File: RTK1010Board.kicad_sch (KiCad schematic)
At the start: 71 parts, among them J1 SMA, J2 IPEX, J3 USB_OTG, J4 BNO055, U1 RTK-1010, U2 MCP1700-3002E_SOT23, U3 MCP1700-3002E_SOT23, U4 ESP32-S2-WROVER

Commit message: some optimiziations implemented
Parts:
- added C12: 10uF, Capacitor_Tantalum_SMD:CP_EIA-7132-20_AVX-U_Pad2.72x3.50mm_HandSolder, symbol Device:C_Polarized_Small
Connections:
- net 5V is gone; now on net U5: JP2.2 (B)
- net GND: now also C12.2
- net U5: now also C12.1
- no-connect marks 25 -> 35
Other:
- note added: "BNO055 IMU (Optional)"
- moved on the sheet: J4, R17, R18

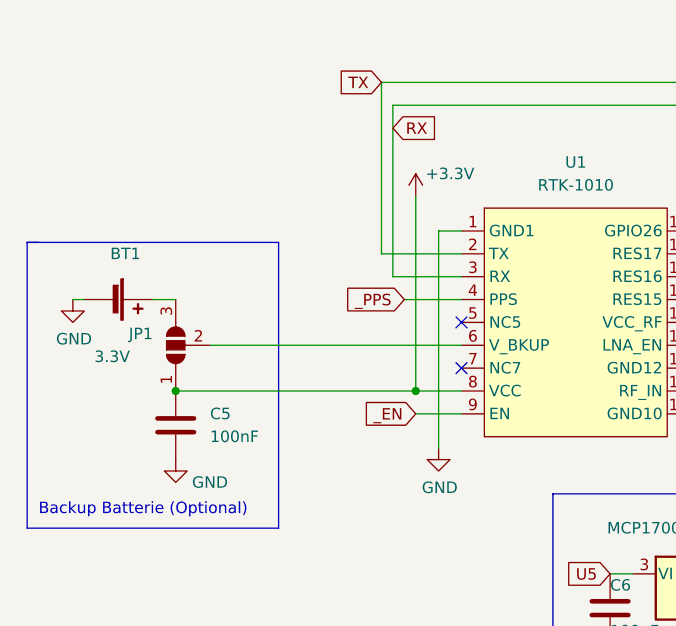
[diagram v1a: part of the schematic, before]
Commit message: RTK1010 VCC LP filter added
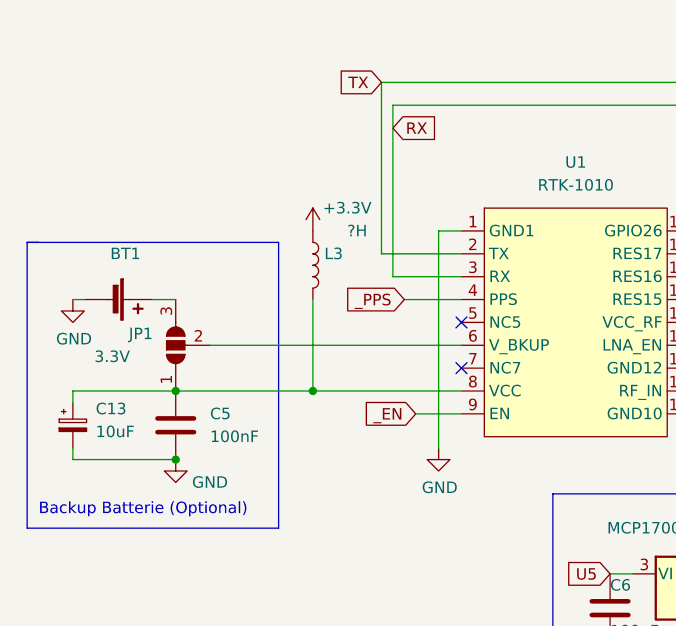
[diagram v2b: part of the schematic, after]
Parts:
- added C13: 10uF, Capacitor_Tantalum_SMD:CP_EIA-7132-20_AVX-U_Pad2.72x3.50mm_HandSolder, symbol Device:C_Polarized_Small
- added L3: ?H, Inductor_SMD:L_0805_2012Metric_Pad1.15x1.40mm_HandSolder, symbol Device:L
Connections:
- net +3V3: now also L3.1; no longer C5.1, JP1.1 (A), U1.8 (VCC)
- net GND: now also C13.2
- new net: C13.1, C5.1, JP1.1 (A), L3.2, U1.8 (VCC)
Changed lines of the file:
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@@
   (junction (at 88.9 85.09) (diameter 0) (color 0 0 0 0)
   )
-  (junction (at 57.15 57.15) (diameter 0) (color 0 0 0 0)
-  )
   (junction (at 275.59 157.48) (diameter 0) (color 0 0 0 0)
   )
@@
   (junction (at 60.96 189.23) (diameter 0) (color 0 0 0 0)
   )
+  (junction (at 45.72 57.15) (diameter 0) (color 0 0 0 0)
+  )
   (junction (at 251.46 157.48) (diameter 0) (color 0 0 0 0)
   )
@@
   (junction (at 177.8 66.04) (diameter 0) (color 0 0 0 0)
   )
+  (junction (at 30.48 64.77) (diameter 0) (color 0 0 0 0)
+  )
   (junction (at 280.67 157.48) (diameter 0) (color 0 0 0 0)
   )
@@
     (stroke (width 0) (type default) (color 0 0 0 0))
   )
-  (wire (pts (xy 57.15 57.15) (xy 62.23 57.15))
+  (wire (pts (xy 30.48 57.15) (xy 45.72 57.15))
     (stroke (width 0) (type default) (color 0 0 0 0))
   )
@@
     (stroke (width 0) (type default) (color 0 0 0 0))
   )
+  (wire (pts (xy 45.72 57.15) (xy 62.23 57.15))
+    (stroke (width 0) (type default) (color 0 0 0 0))
+  )
   (wire (pts (xy 201.93 121.92) (xy 208.28 121.92))
     (stroke (width 0) (type default) (color 0 0 0 0))
@@
     (stroke (width 0) (type default) (color 0 0 0 0))
   )
-  (wire (pts (xy 57.15 35.56) (xy 57.15 57.15))
-    (stroke (width 0) (type default) (color 0 0 0 0))
-  )
   (polyline (pts (xy 233.68 134.62) (xy 233.68 97.79))
     (stroke (width 0) (type default) (color 0 0 0 0))
@@
     (stroke (width 0) (type default) (color 0 0 0 0))
   )
-  (wire (pts (xy 30.48 57.15) (xy 57.15 57.15))
+  (wire (pts (xy 30.48 64.77) (xy 19.05 64.77))
+    (stroke (width 0) (type default) (color 0 0 0 0))
+  )
+  (wire (pts (xy 30.48 57.15) (xy 19.05 57.15))
     (stroke (width 0) (type default) (color 0 0 0 0))
   )
@@
     (stroke (width 0) (type default) (color 0 0 0 0))
   )
+  (wire (pts (xy 19.05 64.77) (xy 19.05 63.5))
+    (stroke (width 0) (type default) (color 0 0 0 0))
+  )
   (wire (pts (xy 201.93 116.84) (xy 217.17 116.84))
     (stroke (width 0) (type default) (color 0 0 0 0))
@@
     (stroke (width 0) (type default) (color 0 0 0 0))
   )
+  (wire (pts (xy 45.72 46.99) (xy 45.72 57.15))
+    (stroke (width 0) (type default) (color 0 0 0 0))
+  )
+  (wire (pts (xy 19.05 57.15) (xy 19.05 58.42))
+    (stroke (width 0) (type default) (color 0 0 0 0))
+  )
   (polyline (pts (xy 46.99 142.24) (xy 46.99 157.48))
     (stroke (width 0) (type default) (color 0 0 0 0))
@@
     (pin "1")
   )
+  (symbol (lib_id "Device:C_Polarized_Small") (at 19.05 60.96 0) (unit 1)
+    (in_bom yes) (on_board yes) (fields_autoplaced)
+    (property "Reference" "C13" (id 0) (at 21.59 59.1438 0)
+      (effects (font (size 1.27 1.27)) (justify left))
+    )
+    (property "Value" "10uF" (id 1) (at 21.59 61.6838 0)
+      (effects (font (size 1.27 1.27)) (justify left))
+    )
+    (property "Footprint" "Capacitor_Tantalum_SMD:CP_EIA-7132-20_AVX-U_Pad2.72x3.50mm_HandSolder" (id 2) (at 19.05 60.96 0)
+      (effects (font (size 1.27 1.27)) hide)
+    )
+    (property "Datasheet" "~" (id 3) (at 19.05 60.96 0)
+      (effects (font (size 1.27 1.27)) hide)
+    )
+    (pin "1")
+    (pin "2")
+  )
   (symbol (lib_id "Device:R") (at 257.81 33.02 270) (unit 1)
     (in_bom yes) (on_board yes)
@@
     (pin "2")
   )
+  (symbol (lib_id "Device:L") (at 45.72 43.18 0) (unit 1)
+    (in_bom yes) (on_board yes)
+    (property "Reference" "L3" (id 0) (at 46.99 41.9099 0)
+      (effects (font (size 1.27 1.27)) (justify left))
+    )
+    (property "Value" "?H" (id 1) (at 49.53 39.37 0)
+      (effects (font (size 1.27 1.27)) (justify left))
+    )
+    (property "Footprint" "Inductor_SMD:L_0805_2012Metric_Pad1.15x1.40mm_HandSolder" (id 2) (at 45.72 43.18 0)
+      (effects (font (size 1.27 1.27)) hide)
+    )
+    (property "Datasheet" "~" (id 3) (at 45.72 43.18 0)
+      (effects (font (size 1.27 1.27)) hide)
+    )
+    (pin "1")
+    (pin "2")
+  )
   (symbol (lib_id "power:+3.3V") (at 256.54 76.2 0) (unit 1)
     (in_bom yes) (on_board yes) (fields_autoplaced)
@@
     (pin "2")
   )
-  (symbol (lib_id "power:+3.3V") (at 57.15 35.56 0) (unit 1)
+  (symbol (lib_id "power:+3.3V") (at 45.72 39.37 0) (unit 1)
     (in_bom yes) (on_board yes)
-    (property "Reference" "#PWR0105" (id 0) (at 57.15 39.37 0)
+    (property "Reference" "#PWR0105" (id 0) (at 45.72 43.18 0)
       (effects (font (size 1.27 1.27)) hide)
     )
-    (property "Value" "+3.3V" (id 1) (at 60.96 33.02 0))
-    (property "Footprint" "" (id 2) (at 57.15 35.56 0)
+    (property "Value" "+3.3V" (id 1) (at 49.53 36.83 0))
+    (property "Footprint" "" (id 2) (at 45.72 39.37 0)
       (effects (font (size 1.27 1.27)) hide)
     )
-    (property "Datasheet" "" (id 3) (at 57.15 35.56 0)
+    (property "Datasheet" "" (id 3) (at 45.72 39.37 0)
       (effects (font (size 1.27 1.27)) hide)
     )
@@
       (reference "C12") (unit 1) (value "10uF") (footprint "Capacitor_Tantalum_SMD:CP_EIA-7132-20_AVX-U_Pad2.72x3.50mm_HandSolder")
     )
+    (path "/230950e4-b3e4-46f1-8b2d-46a20f9cea9a"
+      (reference "C13") (unit 1) (value "10uF") (footprint "Capacitor_Tantalum_SMD:CP_EIA-7132-20_AVX-U_Pad2.72x3.50mm_HandSolder")
+    )
     (path "/d72a6ef7-d3c2-41ed-9dd7-c739e288ebe4"
       (reference "H1") (unit 1) (value "MountingHole_Pad") (footprint "MountingHole:MountingHole_3.2mm_M3_DIN965_Pad")
@@
       (reference "L2") (unit 1) (value "39nH") (footprint "Inductor_SMD:L_0805_2012Metric_Pad1.15x1.40mm_HandSolder")
     )
+    (path "/8422b3d4-486e-4fcf-a47a-02bf73d364a6"
+      (reference "L3") (unit 1) (value "?H") (footprint "Inductor_SMD:L_0805_2012Metric_Pad1.15x1.40mm_HandSolder")
+    )
     (path "/4f96ea1f-44c1-4973-933a-57d8b3b1bc93"

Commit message: Jefs comments implemented
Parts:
- U2, U3: value MCP1700-3002E_SOT23 -> MCP1700-3302E_SOT23
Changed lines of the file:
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@@
     (in_bom yes) (on_board yes)
     (property "Reference" "U3" (id 0) (at 88.9 69.85 0))
-    (property "Value" "MCP1700-3002E_SOT23" (id 1) (at 88.9 72.39 0))
+    (property "Value" "MCP1700-3302E_SOT23" (id 1) (at 88.9 72.39 0))
     (property "Footprint" "Package_TO_SOT_SMD:SOT-23" (id 2) (at 88.9 71.755 0)
       (effects (font (size 1.27 1.27)) hide)
     )
-    (property "Datasheet" "http://ww1.microchip.com/downloads/en/DeviceDoc/20001826D.pdf" (id 3) (at 88.9 77.47 0)
+    (property "Datasheet" "https://www.reichelt.de/de/de/ldo-festspannungsregler-3-3-v-250ma-sot-23-3-pin-mcp-1700-3302-p200923.html?search=mcp1700&&r=1" (id 3) (at 88.9 77.47 0)
       (effects (font (size 1.27 1.27)) hide)
     )
@@
     (in_bom yes) (on_board yes) (fields_autoplaced)
     (property "Reference" "U2" (id 0) (at 196.85 139.7 0))
-    (property "Value" "MCP1700-3002E_SOT23" (id 1) (at 196.85 142.24 0))
+    (property "Value" "MCP1700-3302E_SOT23" (id 1) (at 196.85 142.24 0))
     (property "Footprint" "Package_TO_SOT_SMD:SOT-23" (id 2) (at 196.85 141.605 0)
       (effects (font (size 1.27 1.27)) hide)
     )
-    (property "Datasheet" "http://ww1.microchip.com/downloads/en/DeviceDoc/20001826D.pdf" (id 3) (at 196.85 147.32 0)
+    (property "Datasheet" "https://www.reichelt.de/de/de/ldo-festspannungsregler-3-3-v-250ma-sot-23-3-pin-mcp-1700-3302-p200923.html?search=mcp1700&&r=1" (id 3) (at 196.85 147.32 0)
       (effects (font (size 1.27 1.27)) hide)
     )
@@
     )
     (path "/33ce61d4-ba3e-4c38-98ab-8e02bc72780e"
-      (reference "U2") (unit 1) (value "MCP1700-3002E_SOT23") (footprint "Package_TO_SOT_SMD:SOT-23")
+      (reference "U2") (unit 1) (value "MCP1700-3302E_SOT23") (footprint "Package_TO_SOT_SMD:SOT-23")
     )
     (path "/136d5a82-e181-43d0-94d8-5ca5df3d8b70"
-      (reference "U3") (unit 1) (value "MCP1700-3002E_SOT23") (footprint "Package_TO_SOT_SMD:SOT-23")
+      (reference "U3") (unit 1) (value "MCP1700-3302E_SOT23") (footprint "Package_TO_SOT_SMD:SOT-23")
     )
     (path "/106bf86d-3a9f-4dfb-9733-53a90bce3d15"

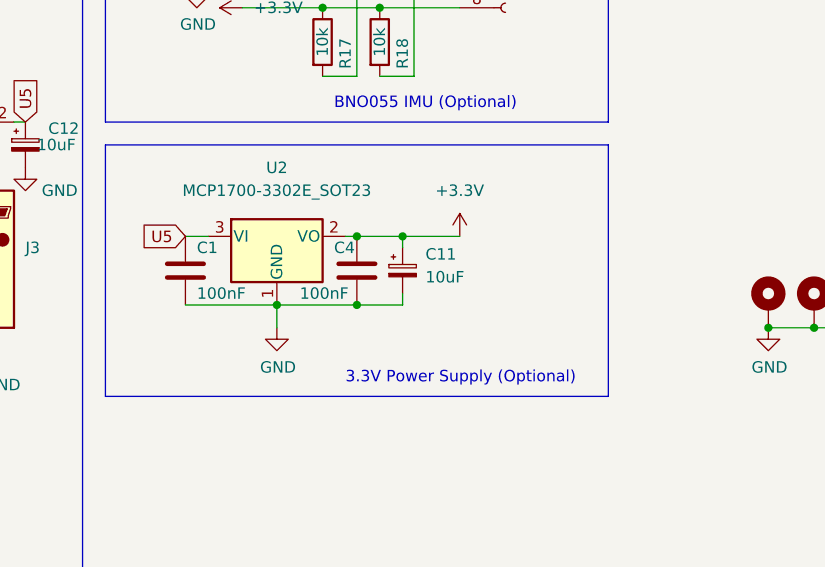
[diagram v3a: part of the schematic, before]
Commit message: LDO replaced by 500ma type
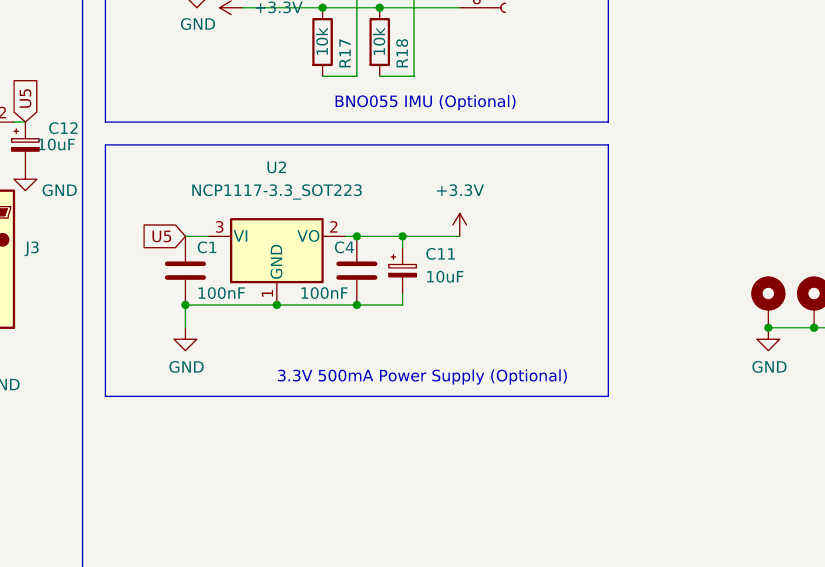
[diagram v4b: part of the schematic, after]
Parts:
- removed U2: MCP1700-3302E_SOT23, Package_TO_SOT_SMD:SOT-23, symbol Regulator_Linear:MCP1700-3002E_SOT23
- added U2: NCP1117-3.3_SOT223, Package_TO_SOT_SMD:SOT-223-3_TabPin2, symbol Regulator_Linear:NCP1117-3.3_SOT223
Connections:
- net +3V3: now also U2.2 (VO)
- net GND: now also U2.1 (GND)
- net U5: now also U2.3 (VI)
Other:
- note added: "3.3V 500mA Power Supply (Optional)"
- note removed: "3.3V Power Supply (Optional)"
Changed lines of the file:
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@@
   (junction (at 205.74 154.94) (diameter 0) (color 0 0 0 0)
   )
+  (junction (at 196.85 154.94) (diameter 0) (color 0 0 0 0)
+  )
   (junction (at 278.13 157.48) (diameter 0) (color 0 0 0 0)
   )
   (junction (at 205.74 147.32) (diameter 0) (color 0 0 0 0)
   )
-  (junction (at 196.85 154.94) (diameter 0) (color 0 0 0 0)
+  (junction (at 186.69 154.94) (diameter 0) (color 0 0 0 0)
   )
   (junction (at 97.79 85.09) (diameter 0) (color 0 0 0 0)
@@
     (stroke (width 0) (type default) (color 0 0 0 0))
   )
+  (wire (pts (xy 196.85 154.94) (xy 205.74 154.94))
+    (stroke (width 0) (type default) (color 0 0 0 0))
+  )
   (polyline (pts (xy 283.21 12.7) (xy 154.94 12.7))
     (stroke (width 0) (type default) (color 0 0 0 0))
@@
     (stroke (width 0) (type default) (color 0 0 0 0))
   )
-  (wire (pts (xy 196.85 154.94) (xy 205.74 154.94))
-    (stroke (width 0) (type default) (color 0 0 0 0))
-  )
   (wire (pts (xy 186.69 154.94) (xy 196.85 154.94))
     (stroke (width 0) (type default) (color 0 0 0 0))
@@
     (stroke (width 0) (type default) (color 0 0 0 0))
   )
-  (wire (pts (xy 196.85 154.94) (xy 196.85 157.48))
+  (wire (pts (xy 186.69 154.94) (xy 186.69 157.48))
     (stroke (width 0) (type default) (color 0 0 0 0))
   )
@@
     (effects (font (size 1.27 1.27)) (justify left bottom))
   )
-  (text "3.3V Power Supply (Optional)\n" (at 204.47 163.83 0)
+  (text "3.3V 500mA Power Supply (Optional)\n" (at 196.85 163.83 0)
     (effects (font (size 1.27 1.27)) (justify left bottom))
   )
@@
     (pin "1")
   )
-  (symbol (lib_id "Regulator_Linear:MCP1700-3002E_SOT23") (at 196.85 147.32 0) (unit 1)
-    (in_bom yes) (on_board yes) (fields_autoplaced)
-    (property "Reference" "U2" (id 0) (at 196.85 139.7 0))
-    (property "Value" "MCP1700-3302E_SOT23" (id 1) (at 196.85 142.24 0))
-    (property "Footprint" "Package_TO_SOT_SMD:SOT-23" (id 2) (at 196.85 141.605 0)
-      (effects (font (size 1.27 1.27)) hide)
-    )
-    (property "Datasheet" "https://www.reichelt.de/de/de/ldo-festspannungsregler-3-3-v-250ma-sot-23-3-pin-mcp-1700-3302-p200923.html?search=mcp1700&&r=1" (id 3) (at 196.85 147.32 0)
-      (effects (font (size 1.27 1.27)) hide)
-    )
-    (pin "1")
-    (pin "2")
-    (pin "3")
-  )
   (symbol (lib_id "power:GND") (at 168.91 139.7 0) (unit 1)
     (in_bom yes) (on_board yes)
@@
     (pin "1")
   )
+  (symbol (lib_id "Regulator_Linear:NCP1117-3.3_SOT223") (at 196.85 147.32 0) (unit 1)
+    (in_bom yes) (on_board yes) (fields_autoplaced)
+    (property "Reference" "U2" (id 0) (at 196.85 139.7 0))
+    (property "Value" "NCP1117-3.3_SOT223" (id 1) (at 196.85 142.24 0))
+    (property "Footprint" "Package_TO_SOT_SMD:SOT-223-3_TabPin2" (id 2) (at 196.85 142.24 0)
+      (effects (font (size 1.27 1.27)) hide)
+    )
+    (property "Datasheet" "http://www.onsemi.com/pub_link/Collateral/NCP1117-D.PDF" (id 3) (at 199.39 153.67 0)
+      (effects (font (size 1.27 1.27)) hide)
+    )
+    (pin "1")
+    (pin "2")
+    (pin "3")
+  )
   (symbol (lib_id "power:+3.3V") (at 149.86 179.07 270) (unit 1)
     (in_bom yes) (on_board yes) (fields_autoplaced)
@@
     (pin "VIN")
   )
-  (symbol (lib_id "power:GND") (at 196.85 157.48 0) (unit 1)
+  (symbol (lib_id "power:GND") (at 186.69 157.48 0) (unit 1)
     (in_bom yes) (on_board yes)
-    (property "Reference" "#PWR0118" (id 0) (at 196.85 163.83 0)
+    (property "Reference" "#PWR0118" (id 0) (at 186.69 163.83 0)
       (effects (font (size 1.27 1.27)) hide)
     )
-    (property "Value" "GND" (id 1) (at 196.977 161.8742 0))
-    (property "Footprint" "" (id 2) (at 196.85 157.48 0)
+    (property "Value" "GND" (id 1) (at 186.817 161.8742 0))
+    (property "Footprint" "" (id 2) (at 186.69 157.48 0)
       (effects (font (size 1.27 1.27)) hide)
     )
-    (property "Datasheet" "" (id 3) (at 196.85 157.48 0)
+    (property "Datasheet" "" (id 3) (at 186.69 157.48 0)
       (effects (font (size 1.27 1.27)) hide)
     )
@@
       (reference "U1") (unit 1) (value "RTK-1010") (footprint "locosystech:rtk1010")
     )
-    (path "/33ce61d4-ba3e-4c38-98ab-8e02bc72780e"
-      (reference "U2") (unit 1) (value "MCP1700-3302E_SOT23") (footprint "Package_TO_SOT_SMD:SOT-23")
+    (path "/4106de16-4ed2-476f-98c7-6e12ffdc75b1"
+      (reference "U2") (unit 1) (value "NCP1117-3.3_SOT223") (footprint "Package_TO_SOT_SMD:SOT-223-3_TabPin2")
     )
     (path "/136d5a82-e181-43d0-94d8-5ca5df3d8b70"

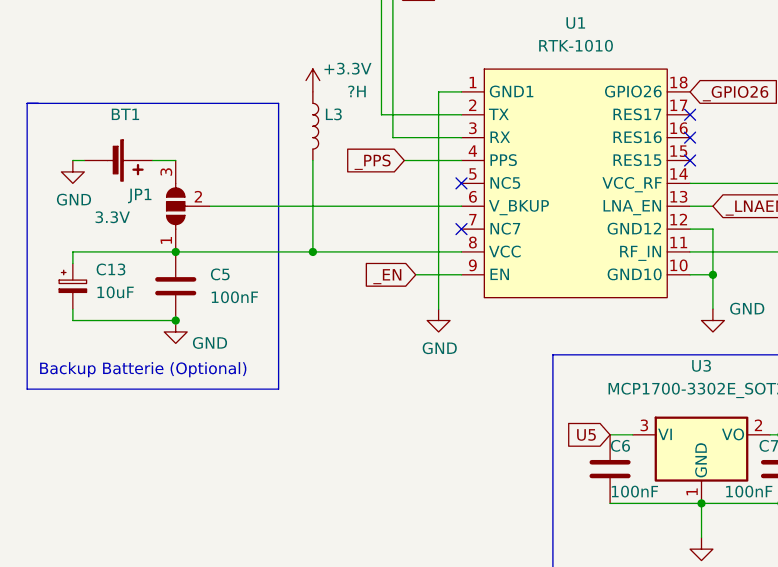
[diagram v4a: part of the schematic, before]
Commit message: support for teseo-liv3fl added
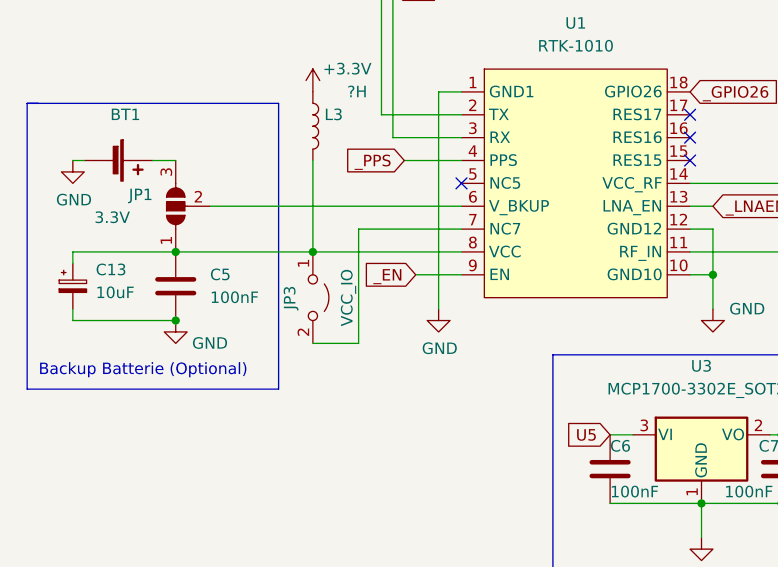
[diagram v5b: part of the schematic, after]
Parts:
- added JP3: VCC_IO, Jumper:SolderJumper-2_P1.3mm_Open_RoundedPad1.0x1.5mm, symbol Jumper:Jumper_2_Open
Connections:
- net at C13.1, C5.1, JP1.1 (A)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: now also JP3.1 (A)
- net at U1.7 (NC7): now also JP3.2 (B)
- no-connect marks 35 -> 34
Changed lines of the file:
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@@
   (no_connect (at 181.61 55.88))
   (no_connect (at 181.61 40.64))
-  (no_connect (at 62.23 54.61))
   (no_connect (at 87.63 44.45))
   (no_connect (at 181.61 43.18))
@@
   (no_connect (at 133.35 181.61))
   (no_connect (at 181.61 71.12))
+  (wire (pts (xy 62.23 54.61) (xy 50.8 54.61))
+    (stroke (width 0) (type default) (color 0 0 0 0))
+  )
   (wire (pts (xy 55.88 119.38) (xy 60.96 119.38))
     (stroke (width 0) (type default) (color 0 0 0 0))
@@
     (stroke (width 0) (type default) (color 0 0 0 0))
   )
+  (wire (pts (xy 50.8 67.31) (xy 45.72 67.31))
+    (stroke (width 0) (type default) (color 0 0 0 0))
+  )
   (wire (pts (xy 57.15 109.22) (xy 60.96 109.22))
     (stroke (width 0) (type default) (color 0 0 0 0))
@@
     (stroke (width 0) (type default) (color 0 0 0 0))
   )
+  (wire (pts (xy 50.8 54.61) (xy 50.8 67.31))
+    (stroke (width 0) (type default) (color 0 0 0 0))
+  )
   (wire (pts (xy 30.48 64.77) (xy 19.05 64.77))
     (stroke (width 0) (type default) (color 0 0 0 0))
@@
     (pin "2")
   )
+  (symbol (lib_id "Jumper:Jumper_2_Open") (at 45.72 62.23 270) (unit 1)
+    (in_bom yes) (on_board yes)
+    (property "Reference" "JP3" (id 0) (at 43.18 62.23 0))
+    (property "Value" "VCC_IO" (id 1) (at 49.53 62.23 0))
+    (property "Footprint" "Jumper:SolderJumper-2_P1.3mm_Open_RoundedPad1.0x1.5mm" (id 2) (at 45.72 62.23 0)
+      (effects (font (size 1.27 1.27)) hide)
+    )
+    (property "Datasheet" "~" (id 3) (at 45.72 62.23 0)
+      (effects (font (size 1.27 1.27)) hide)
+    )
+    (pin "1")
+    (pin "2")
+  )
   (symbol (lib_id "Device:C") (at 57.15 181.61 0) (unit 1)
     (in_bom yes) (on_board yes) (fields_autoplaced)
@@
       (reference "JP2") (unit 1) (value "USB power") (footprint "Jumper:SolderJumper-2_P1.3mm_Open_RoundedPad1.0x1.5mm")
     )
+    (path "/70b11c5c-a29b-4348-a736-0eb2e4eb067e"
+      (reference "JP3") (unit 1) (value "VCC_IO") (footprint "Jumper:SolderJumper-2_P1.3mm_Open_RoundedPad1.0x1.5mm")
+    )
     (path "/9bbf26c0-e794-41fd-abca-b77796fb1d09"
